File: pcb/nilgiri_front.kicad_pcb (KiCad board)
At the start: 2 copper layers, 100 x 65.7 mm, 4 parts

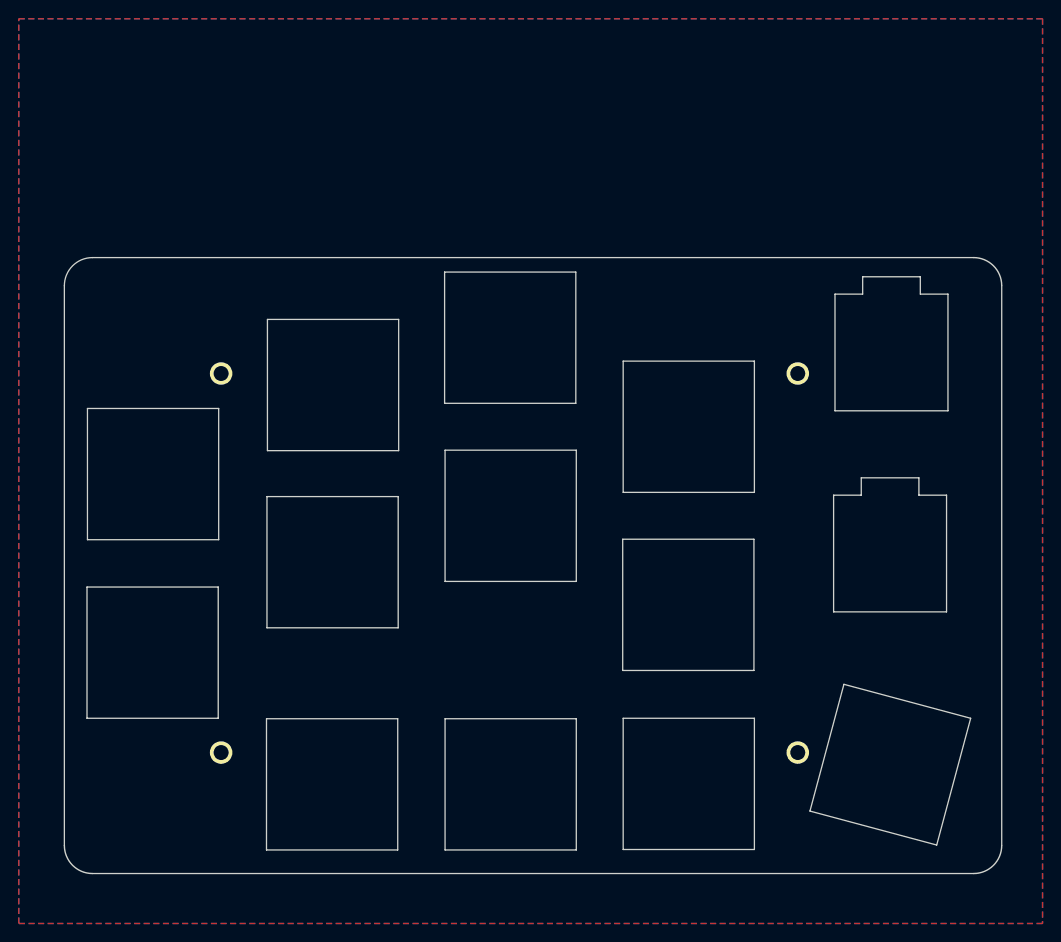
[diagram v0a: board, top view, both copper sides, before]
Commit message: fixed front panel
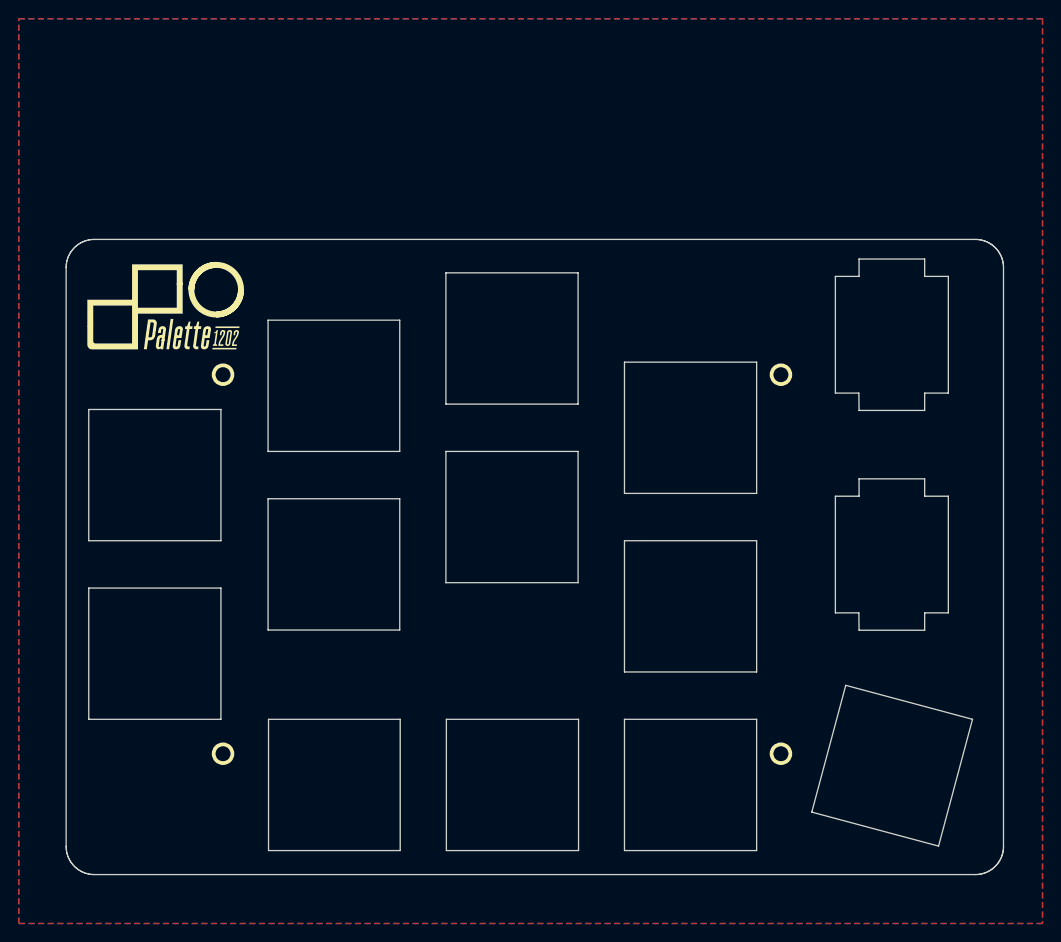
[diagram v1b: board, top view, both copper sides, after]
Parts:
- moved H7 1.80 mm to (162.6, 71.0)
- moved H8 1.80 mm to (162.6, 111.4)
- moved H5 0.24 mm to (103.1, 71.0)
- moved H6 0.24 mm to (103.1, 111.4)
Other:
- board size 100 x 65.7 mm -> 100 x 67.8 mm
- board text removed: "are not correct, except key switches."
- board text removed: "note: the positions or sizes"
- board text removed: "shaft:7mm"
